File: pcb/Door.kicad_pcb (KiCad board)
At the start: 2 copper layers, 20.3 x 57.1 mm, 27 parts, among them J101 Programming, J102 Battery input, Q101 IRLML6402, Q201 BSS83P, Q202 BC817, SW101 FLASH, SW102 RESET, SW103 SW_Reed, U101 ESP-12F, U301 TPL5110

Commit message: Changed directory structure
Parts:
- removed Q101: IRLML6402, Package_TO_SOT_SMD:SOT-23
- removed R107: 10K, Resistor_SMD:R_0805_2012Metric
- added Q301: IRLML6402, Package_TO_SOT_SMD:SOT-23, F.Cu at (148.6, 98.3)
- added R302: 10K, Resistor_SMD:R_0805_2012Metric, F.Cu at (138.9, 93.7)
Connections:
- net /GP15 renamed Net-(R106-Pad2)
- R108 pad 1: GND -> /GP_TIMER
- R108 pad 2: /GP_TIMER -> GND
- U301 pad 5: /timer/DRV_OUT -> Net-(R302-Pad2)
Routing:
- net /timer/DRV_OUT: track 18.2 -> 0.00 mm, vias 2 -> 0
- net Net-(R302-Pad2): track 0.00 -> 17.8 mm, vias 0 -> 2
- net Net-(Q301-Pad1): track 0.00 -> 13.3 mm, vias 0 -> 2
- net Net-(Q101-Pad1): track 13.3 -> 0.00 mm, vias 2 -> 0
- net GND: track 132.2 -> 128.7 mm, vias 2 -> 5
- net /GP_TIMER: track 30.6 -> 32.1 mm
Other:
- board text added: "REV 1.2"
- board text removed: "REV 1.1"

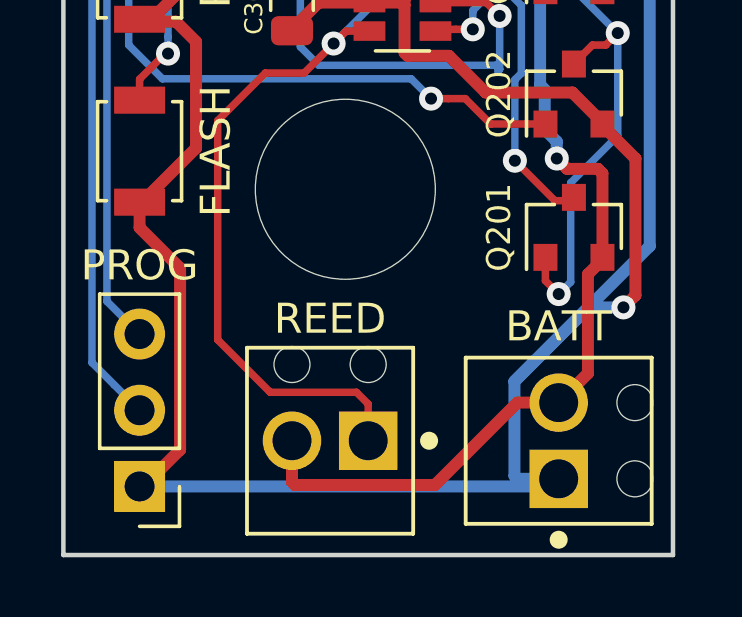
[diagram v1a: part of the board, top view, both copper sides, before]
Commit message: Hole clearance update
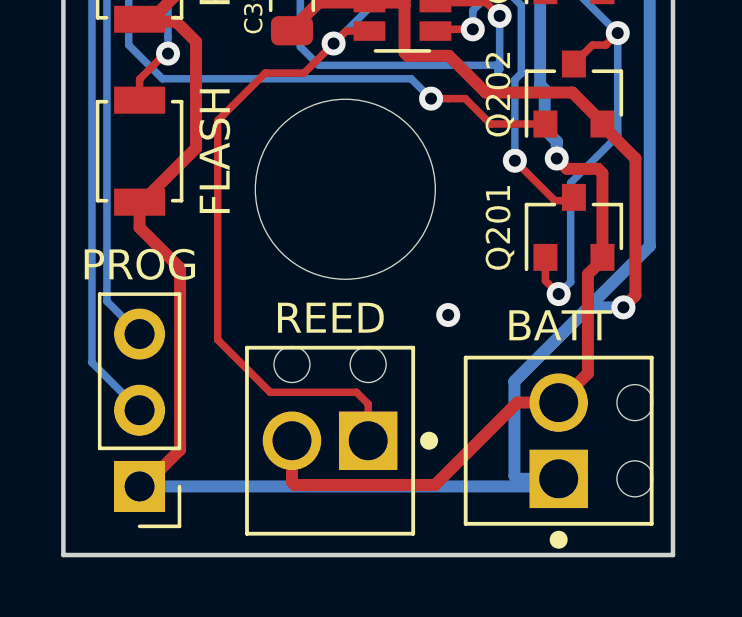
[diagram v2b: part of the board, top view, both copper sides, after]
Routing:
- net GND: vias 5 -> 6
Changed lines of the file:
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@@
     (thickness 1.6)
     (drawings 13)
-    (tracks 394)
+    (tracks 395)
     (zones 0)
     (modules 27)
@@
   (module ViktorStiskala:M6_Hole (layer F.Cu)
     (at 140.97 105.918)
+    (solder_mask_margin 0.2)
+    (clearance 0.3)
     (fp_text reference REF** (at 0 4) (layer F.SilkS) hide
       (effects (font (size 1 1) (thickness 0.15)))
@@
   (via (at 137.287 75.946) (size 0.8) (drill 0.4) (layers F.Cu B.Cu) (net 2))
   (via (at 143.129 76.708) (size 0.8) (drill 0.4) (layers F.Cu B.Cu) (net 2))
+  (via (at 144.399 110.109) (size 0.8) (drill 0.4) (layers F.Cu B.Cu) (net 2))
   (via (at 146.812 70.104) (size 0.8) (drill 0.4) (layers F.Cu B.Cu) (net 3))
   (segment (start 147.211999 69.704001) (end 149.206001 69.704001) (width 0.25) (layer F.Cu) (net 3) (status 20))
@@
   (segment (start 133.023849 109.655849) (end 133.023849 91.005561) (width 0.25) (layer B.Cu) (net 4))
   (segment (start 146.412001 72.027999) (end 146.812 71.628) (width 0.25) (layer B.Cu) (net 4))
-  (via (at 146.1135 100.1395) (size 0.8) (drill 0.4) (layers F.Cu B.Cu) (net 19))
-  (segment (start 145.669 99.695) (end 146.1135 100.1395) (width 0.25) (layer F.Cu) (net 19))
-  (segment (start 143.975 99.695) (end 145.669 99.695) (width 0.25) (layer F.Cu) (net 19) (status 10))
-  (segment (start 146.1135 100.1395) (end 146.1135 101.9175) (width 0.25) (layer B.Cu) (net 19))
-  (segment (start 146.1135 101.9175) (end 146.05 101.981) (width 0.25) (layer B.Cu) (net 19))
   (via (at 150.0505 100.711) (size 0.8) (drill 0.4) (layers F.Cu B.Cu) (net 5))
   (segment (start 148.5265 99.187) (end 150.0505 100.711) (width 0.25) (layer B.Cu) (net 5))
@@
   (segment (start 146.6215 75.1205) (end 148.0185 73.7235) (width 0.25) (layer F.Cu) (net 12))
   (segment (start 148.0185 73.7235) (end 149.225 73.7235) (width 0.25) (layer F.Cu) (net 12) (status 20))
-  (segment (start 151.007001 82.811999) (end 149.856002 81.661) (width 0.25) (layer F.Cu) (net 18) (status 20))
-  (segment (start 151.007001 87.534499) (end 151.007001 82.811999) (width 0.25) (layer F.Cu) (net 18))
-  (segment (start 150.114 88.4275) (end 151.007001 87.534499) (width 0.25) (layer F.Cu) (net 18) (status 10))
-  (segment (start 149.856002 81.661) (end 149.479 81.661) (width 0.25) (layer F.Cu) (net 18) (status 30))
   (segment (start 141.9225 92.9005) (end 141.859 92.9005) (width 0.25) (layer F.Cu) (net 13) (status 30))
   (segment (start 141.732 92.7885) (end 143.066289 94.122789) (width 0.25) (layer F.Cu) (net 13) (status 10))
@@
   (segment (start 145.770687 98.806) (end 145.205002 98.806) (width 0.25) (layer F.Cu) (net 17))
   (segment (start 146.262687 99.298) (end 145.770687 98.806) (width 0.25) (layer F.Cu) (net 17))
+  (segment (start 151.007001 82.811999) (end 149.856002 81.661) (width 0.25) (layer F.Cu) (net 18) (status 20))
+  (segment (start 151.007001 87.534499) (end 151.007001 82.811999) (width 0.25) (layer F.Cu) (net 18))
+  (segment (start 150.114 88.4275) (end 151.007001 87.534499) (width 0.25) (layer F.Cu) (net 18) (status 10))
+  (segment (start 149.856002 81.661) (end 149.479 81.661) (width 0.25) (layer F.Cu) (net 18) (status 30))
+  (via (at 146.1135 100.1395) (size 0.8) (drill 0.4) (layers F.Cu B.Cu) (net 19))
+  (segment (start 145.669 99.695) (end 146.1135 100.1395) (width 0.25) (layer F.Cu) (net 19))
+  (segment (start 143.975 99.695) (end 145.669 99.695) (width 0.25) (layer F.Cu) (net 19) (status 10))
+  (segment (start 146.1135 100.1395) (end 146.1135 101.9175) (width 0.25) (layer B.Cu) (net 19))
+  (segment (start 146.1135 101.9175) (end 146.05 101.981) (width 0.25) (layer B.Cu) (net 19))
   (segment (start 139.471908 96.69915) (end 139.471908 96.133465) (width 0.25) (layer B.Cu) (net 19))
   (segment (start 146.1135 101.9175) (end 145.980989 101.784989) (width 0.25) (layer B.Cu) (net 19))
